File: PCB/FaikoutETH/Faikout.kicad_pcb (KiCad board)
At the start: 2 copper layers, 70 x 70 mm, 73 parts, among them J1 1x5, J2 TC2030-USB-NL, J3 Reset, J4 RJ45_LED, Q1 BSS138PS, U1 KSZ8851SNL, U4 ESP32-S3-MINI-1, U5 TPS62933, Y1 Crystal_GND24

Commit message: As ordered
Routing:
- net D+: track 42.1 -> 42.6 mm

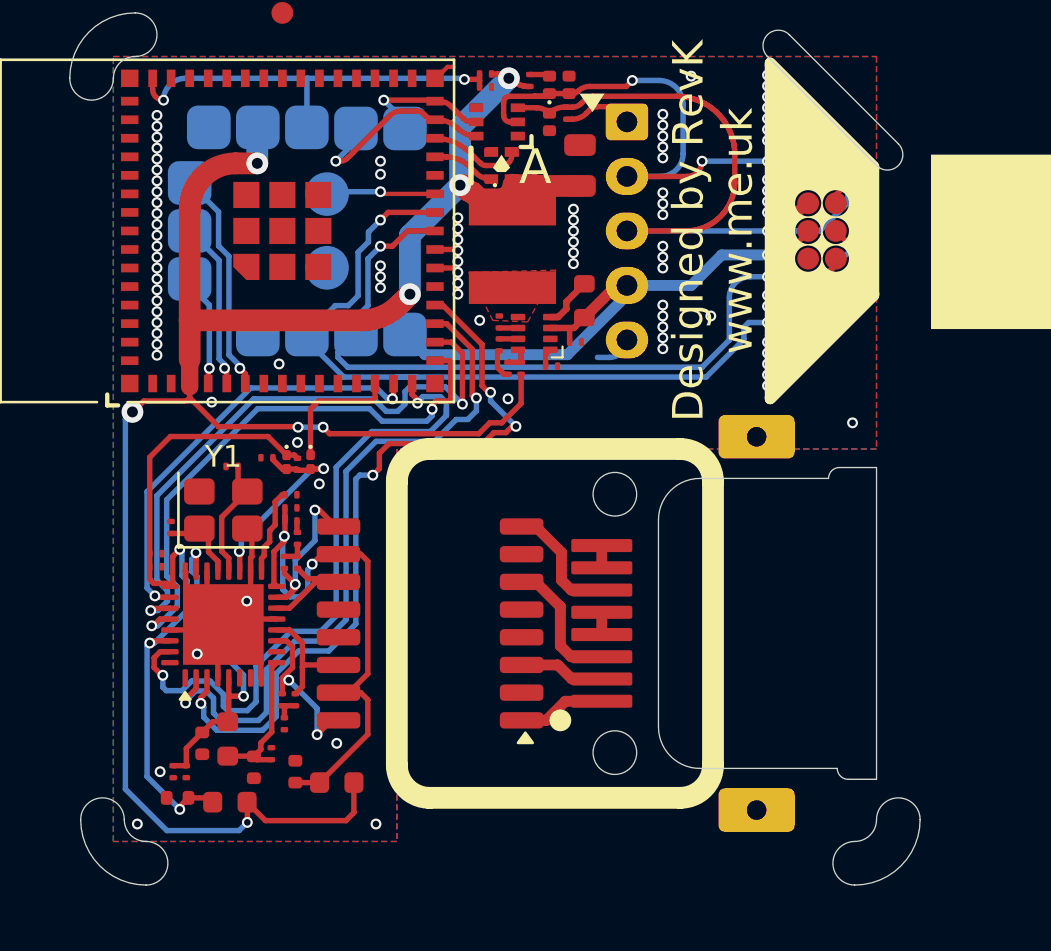
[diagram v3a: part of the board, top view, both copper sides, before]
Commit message: New inductor
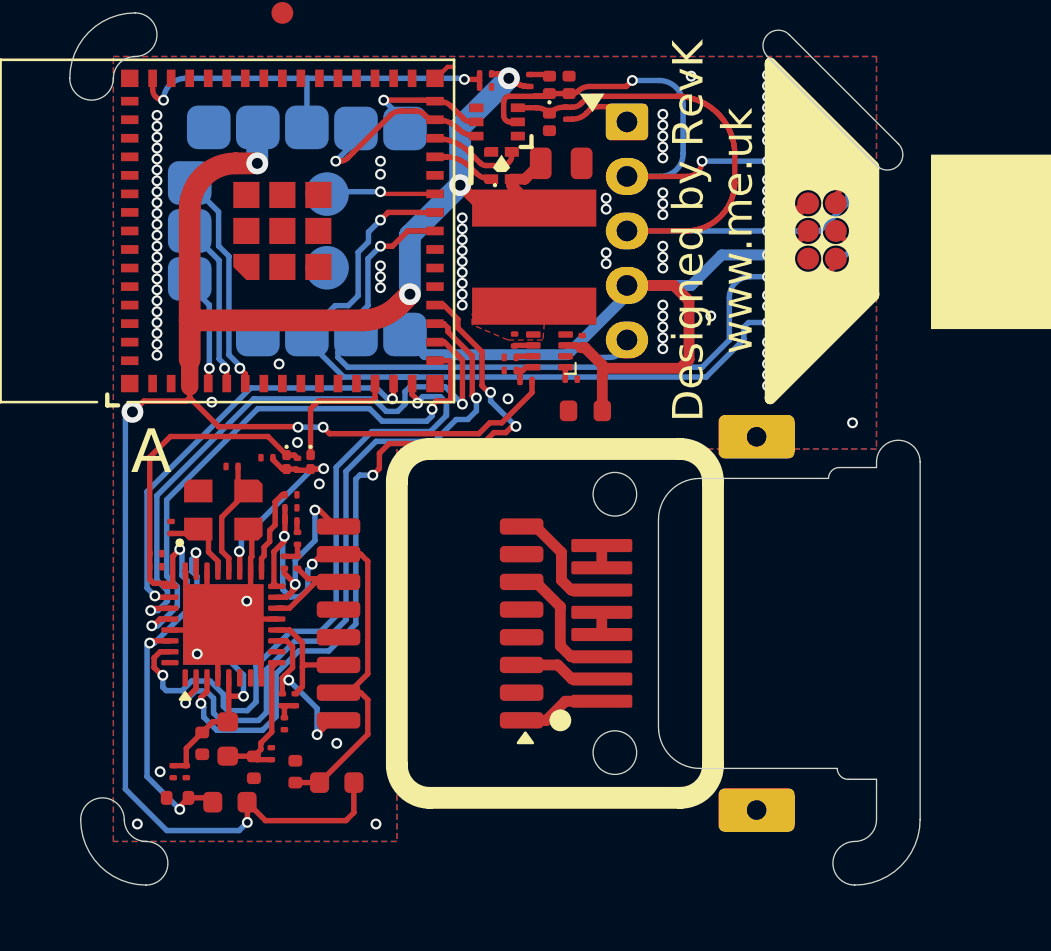
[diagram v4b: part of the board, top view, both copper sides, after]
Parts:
- removed C29: 10uF 35V, RevK:C_0603
- removed C30, C32: 100nF 35V, RevK:C_0201
- removed C31: 33nF, RevK:C_0201
- removed C33: 100uF 6.3V, RevK:C_0805
- removed L13: 4.7uH, RevK:L_5x5
- removed R15: 33k, RevK:R_0201
- removed R16: 30.9k 1%, RevK:R_0201
- removed R17: 10k, RevK:R_0201
- removed U5: TPS62933, RevK:SOT-583-8
- added C1: 10uF 35V, RevK:C_0603, F.Cu at (143.7, 63.2)
- added C2: 100nF 35V, RevK:C_0201, F.Cu at (143.5, 60.1)
- added C3: 33nF, RevK:C_0201, F.Cu at (140.2, 60.8)
- added C4: 100nF 35V, RevK:C_0201, F.Cu at (140.4, 60.0)
- added C5: 100uF 6.3V, RevK:C_0805, F.Cu at (142.5, 51.9)
- added L1: 4.7uH, RevK:L_6x6, F.Cu at (141.3, 56.2)
- added R5: 33k, RevK:R_0201, F.Cu at (143.0, 61.8)
- added R6: 30.9k 1%, RevK:R_0201, F.Cu at (140.9, 61.9)
- added R8: 10k, RevK:R_0201, F.Cu at (140.2, 61.4)
- added U2: TPS62933, RevK:SOT-583-8, F.Cu at (142.0, 60.5)
- U1: footprint RevK:QFN-32-1EP_5x5mm_P0.5mm_EP3.7x3.7mm-hot -> RevK:QFN-32-1EP_5x5mm_P0.5mm_EP3.7x3.7mm
- Y1: footprint Crystal:Crystal_SMD_3225-4Pin_3.2x2.5mm -> RevK:Crystal-3.2x2.5
- turned Y1 to 180 degrees
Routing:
- net DC: track 27.2 -> 37.0 mm
- net GND: track 34.2 -> 24.7 mm, vias 91 -> 89
- net +3.3V: track 100.1 -> 98.2 mm

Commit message: Tweaks
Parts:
- U1: footprint RevK:QFN-32-1EP_5x5mm_P0.5mm_EP3.7x3.7mm -> RevK:QFN-32-1EP_5x5mm_P0.5mm_EP3.7x3.7mm-hot
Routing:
- net DC: track 37.0 -> 42.5 mm
- net GND: track 24.7 -> 23.0 mm, vias 89 -> 88
- net +1V8: track 15.0 -> 16.4 mm
- net D-: track 34.4 -> 35.3 mm
- net D+: track 42.6 -> 43.4 mm
- net SI: track 30.7 -> 29.9 mm
